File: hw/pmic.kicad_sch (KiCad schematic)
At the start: 36 parts, among them J1 TYPE-C-31-M-13C, J2 Conn_01x02, U2 NPM1300-QEAA-R

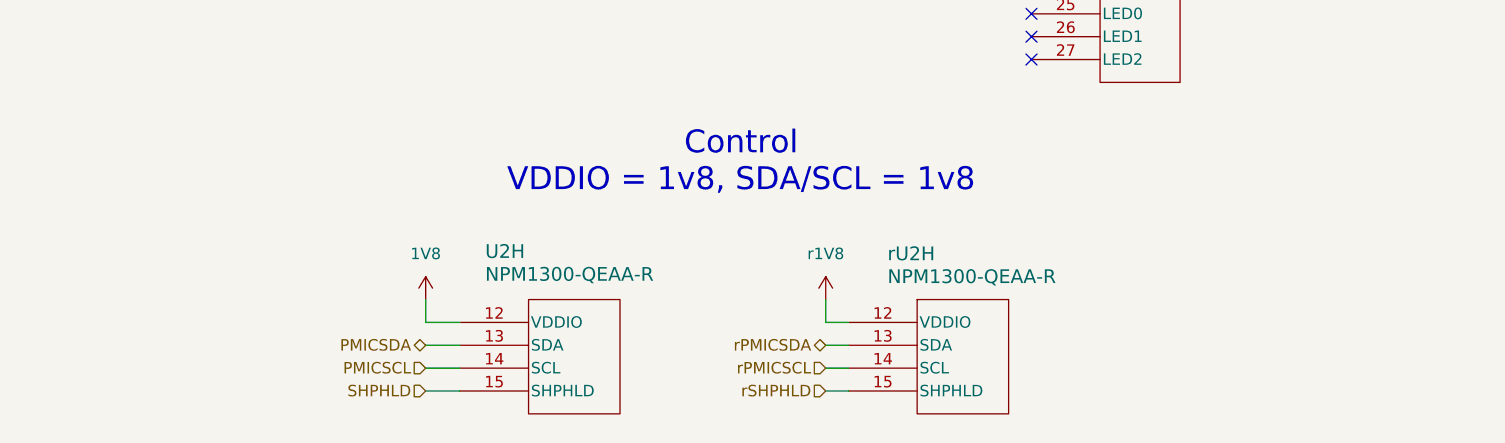
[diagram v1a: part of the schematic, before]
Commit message: Hook up mcu
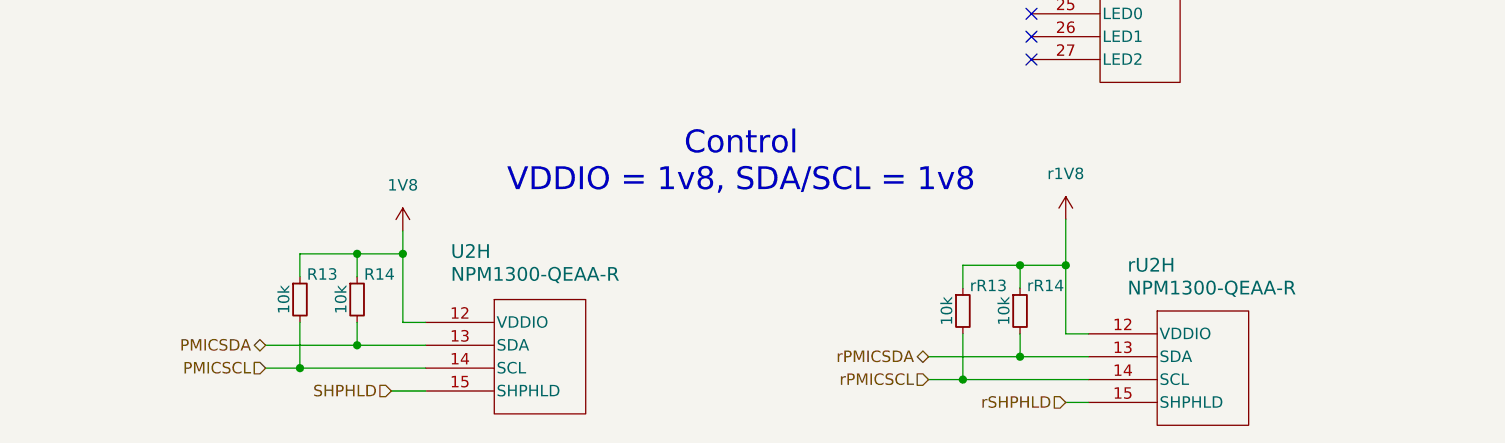
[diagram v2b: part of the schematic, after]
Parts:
- added R13, R14, rR13, rR14: 10k, symbol Alidade:R
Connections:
- net 1V8: now also R13.1, R14.1
- net PMICSCL: now also R13.2
- net PMICSDA: now also R14.2
- net r1V8: now also rR13.1, rR14.1
- net rPMICSCL: now also rR13.2
- net rPMICSDA: now also rR14.2
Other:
- moved on the sheet: U2H, rU2H

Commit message: Debug header
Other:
- title: (none) -> Alidade
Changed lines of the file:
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@@
 	(generator_version "9.0")
 	(paper "A3")
+	(title_block
+		(title "Alidade")
+		(date "2026-03-29")
+		(rev "1.0.0rc1")
+	)
 	(text "Unregulated Power and Ground"
 		(exclude_from_sim no)
@@
 	(wire
 		(pts
-			(xy 290.83 247.65) (xy 293.37 247.65)
+			(xy 275.59 247.65) (xy 293.37 247.65)
 		)
 		(stroke
@@
 	(wire
 		(pts
-			(xy 215.9 246.38) (xy 219.71 246.38)
+			(xy 201.93 246.38) (xy 219.71 246.38)
 		)
 		(stroke
@@
 	(hierarchical_label "SHPHLD"
 		(shape input)
-		(at 215.9 246.38 180)
+		(at 201.93 246.38 180)
 		(effects
 			(font
@@
 	(hierarchical_label "rSHPHLD"
 		(shape input)
-		(at 290.83 247.65 180)
-		(effects
-			(font
+		(at 275.59 247.65 180)
+		(effects
+			(font
